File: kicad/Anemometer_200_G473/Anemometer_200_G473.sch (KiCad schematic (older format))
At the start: 147 parts, among them J1 Conn_01x01_Female, J11 USB_B_Micro, J13 Conn_01x01_Female, J15 Conn_01x01_Female, J16 Conn_01x01_Female, J17 Conn_01x01_Female, J18 Conn_01x01_Female, J19 Conn_01x01_Female, J2 Conn_01x01_Female, J20 Conn_01x01_Female, J21 Conn_01x01_Female, J22 Conn_01x01_Female, J23 Conn_01x01_Female, J24 Conn_01x01_Female, J3 Conn_01x08_Shielded, J4 Conn_01x01_Female, J5 Conn_01x01_Female, J6 Conn_01x01_Female, J7 Conn_01x01_Female, J8 Conn_01x04_Shielded, J9 Conn_01x01_Female, Q1 Q_NMOS_GSD, Q2 Q_NMOS_GSD, Q3 Q_NMOS_GSD, Q4 Q_NMOS_GSD, Q5 IRF7343PBF, Q6 IRF7343PBF, Q7 IRF7343PBF, Q8 IRF7343PBF, U1 W5500, U2 NCP1117-3.3, U3 TS5A23159DGS, U4 TS5A23159DGS, Y1 16, Y2 Crystal_GND24_Small

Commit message: изменено:      kicad/Anemometer_200_G473/Anemometer_200_G473-cache.lib 	изменено:      kicad/Anemometer_200_G473/Anemometer_200_G473.kicad_pcb 	изменено:      kicad/Anemometer_200_G473/Anemometer_200_G473.kicad_pcb-bak 	изменено:      kicad/Anemometer_200_G473/Anemometer_200_G473.sch 	изменено:      kicad/Anemometer_200_G473/Anemometer_200_G473.sch-bak
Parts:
- D10: symbol Anemometer_200_G473-rescue:AD5245-My_Library-My_Library -> Anemometer_200_G473-rescue:AD5245-My_Library-My_Library-Anemometer_200_G473-rescue
- D2: symbol Anemometer_200_G473-rescue:STM32G473CBTx-My_Library-Anemometer_200_G473-rescue -> Anemometer_200_G473-rescue:STM32G473CBTx-My_Library-Anemometer_200_G473-rescue-Anemometer_200_G473-rescue
- D5: symbol Anemometer_200_G473-rescue:CH340N-My_Library-Anemometer_200_G473-rescue -> Anemometer_200_G473-rescue:CH340N-My_Library-Anemometer_200_G473-rescue-Anemometer_200_G473-rescue
- D9: symbol Anemometer_200_G473-rescue:MAX4477-My_Library -> Anemometer_200_G473-rescue:MAX4477-My_Library-Anemometer_200_G473-rescue
- J3: symbol Anemometer_200_G473-rescue:Conn_01x08_Shielded-My_Library-Anemometer_200_G473-rescue -> Anemometer_200_G473-rescue:Conn_01x08_Shielded-My_Library-Anemometer_200_G473-rescue-Anemometer_200_G473-rescue
- J8: symbol Anemometer_200_G473-rescue:Conn_01x04_Shielded-My_Library-Anemometer_200_G473-rescue -> Anemometer_200_G473-rescue:Conn_01x04_Shielded-My_Library-Anemometer_200_G473-rescue-Anemometer_200_G473-rescue
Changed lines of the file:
@@
 $EndDescr
 $Comp
-L Anemometer_200_G473-rescue:STM32G473CBTx-My_Library-Anemometer_200_G473-rescue D2
+L Anemometer_200_G473-rescue:STM32G473CBTx-My_Library-Anemometer_200_G473-rescue-Anemometer_200_G473-rescue D2
 U 1 1 645A79A7
 P 8000 2250
@@
 NoConn ~ 8700 1950
 $Comp
-L Anemometer_200_G473-rescue:CH340N-My_Library-Anemometer_200_G473-rescue D5
+L Anemometer_200_G473-rescue:CH340N-My_Library-Anemometer_200_G473-rescue-Anemometer_200_G473-rescue D5
 U 1 1 6496EE1B
 P 9950 2850
@@
 $EndComp
 $Comp
-L Anemometer_200_G473-rescue:Conn_01x08_Shielded-My_Library-Anemometer_200_G473-rescue J3
+L Anemometer_200_G473-rescue:Conn_01x08_Shielded-My_Library-Anemometer_200_G473-rescue-Anemometer_200_G473-rescue J3
 U 1 1 65094C58
 P 5450 1800
@@
 $EndComp
 $Comp
-L Anemometer_200_G473-rescue:Conn_01x04_Shielded-My_Library-Anemometer_200_G473-rescue J8
+L Anemometer_200_G473-rescue:Conn_01x04_Shielded-My_Library-Anemometer_200_G473-rescue-Anemometer_200_G473-rescue J8
 U 1 1 648B00AE
 P 6200 900
@@
 $EndComp
 $Comp
-L Anemometer_200_G473-rescue:MAX4477-My_Library D9
+L Anemometer_200_G473-rescue:MAX4477-My_Library-Anemometer_200_G473-rescue D9
 U 1 1 64A019B6
 P 8050 5150
@@
 $EndComp
 $Comp
-L Anemometer_200_G473-rescue:MAX4477-My_Library D9
+L Anemometer_200_G473-rescue:MAX4477-My_Library-Anemometer_200_G473-rescue D9
 U 2 1 64A0390D
 P 10050 5800
@@
 $EndComp
 $Comp
-L Anemometer_200_G473-rescue:AD5245-My_Library-My_Library D10
+L Anemometer_200_G473-rescue:AD5245-My_Library-My_Library-Anemometer_200_G473-rescue D10
 U 1 1 64A1FA03
 P 8650 5550

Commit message: изменено:      kicad/Anemometer_200_G473/Anemometer_200_G473-cache.lib 	изменено:      kicad/Anemometer_200_G473/Anemometer_200_G473.sch 	изменено:      kicad/Anemometer_200_G473/Anemometer_200_G473.sch-bak 	изменено:      stm32cubeide/Anemometer_G474CBT6_MATLAB/.mxproject 	изменено:      stm32cubeide/Anemometer_G474CBT6_MATLAB/.settings/language.settings.xml 	изменено:      stm32cubeide/Anemometer_G474CBT6_MATLAB/Anemometer_G473CBT7_MATLAB.ioc 	изменено:      stm32cubeide/Anemometer_G474CBT6_MATLAB/Core/Inc/main.h 	изменено:      stm32cubeide/Anemometer_G474CBT6_MATLAB/Core/Inc/stm32g4xx_hal_conf.h 	изменено:      stm32cubeide/Anemometer_G474CBT6_MATLAB/Core/Src/main.c 	изменено:      stm32cubeide/Anemometer_G474CBT6_MATLAB/Debug/Anemometer_G473CBT7_MATLAB.elf 	изменено:      stm32cubeide/Anemometer_G474CBT6_MATLAB/Debug/Anemometer_G473CBT7_MATLAB.list 	изменено:      stm32cubeide/Anemometer_G474CBT6_MATLAB/Debug/Anemometer_G473CBT7_MATLAB.map 	изменено:      stm32cubeide/Anemometer_G474CBT6_MATLAB/Debug/Core/Src/main.cyclo 	изменено:      stm32cubeide/Anemometer_G474CBT6_MATLAB/Debug/Core/Src/main.d 	изменено:      stm32cubeide/Anemometer_G474CBT6_MATLAB/Debug/Core/Src/main.o 	изменено:      stm32cubeide/Anemometer_G474CBT6_MATLAB/Debug/Core/Src/main.su 	изменено:      stm32cubeide/Anemometer_G474CBT6_MATLAB/Debug/Core/Src/stm32g4xx_hal_msp.cyclo 	изменено:      stm32cubeide/Anemometer_G474CBT6_MATLAB/Debug/Core/Src/stm32g4xx_hal_msp.d 	изменено:      stm32cubeide/Anemometer_G474CBT6_MATLAB/Debug/Core/Src/stm32g4xx_hal_msp.o 	изменено:      stm32cubeide/Anemometer_G474CBT6_MATLAB/Debug/Core/Src/stm32g4xx_hal_msp.su 	изменено:      stm32cubeide/Anemometer_G474CBT6_MATLAB/Debug/Core/Src/stm32g4xx_it.cyclo 	изменено:      stm32cubeide/Anemometer_G474CBT6_MATLAB/Debug/Core/Src/stm32g4xx_it.d 	изменено:      stm32cubeide/Anemometer_G474CBT6_MATLAB/Debug/Core/Src/stm32g4xx_it.o 	изменено:      stm32cubeide/Anemometer_G474CBT6_MATLAB/Debug/Core/Src/stm32g4xx_it.su 	измен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
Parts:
- D10: symbol Anemometer_200_G473-rescue:AD5245-My_Library-My_Library-Anemometer_200_G473-rescue -> Anemometer_200_G473-rescue:AD5245-My_Library-My_Library-Anemometer_200_G473-rescue-Anemometer_200_G473-rescue
- D2: symbol Anemometer_200_G473-rescue:STM32G473CBTx-My_Library-Anemometer_200_G473-rescue-Anemometer_200_G473-rescue -> Anemometer_200_G473-rescue:STM32G473CBTx-My_Library-Anemometer_200_G473-rescue-Anemometer_200_G473-rescue-Anemometer_20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
- D5: symbol Anemometer_200_G473-rescue:CH340N-My_Library-Anemometer_200_G473-rescue-Anemometer_200_G473-rescue -> Anemometer_200_G473-rescue:CH340N-My_Library-Anemometer_200_G473-rescue-Anemometer_200_G473-rescue-Anemometer_200_G473-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
- D9: symbol Anemometer_200_G473-rescue:MAX4477-My_Library-Anemometer_200_G473-rescue -> Anemometer_200_G473-rescue:MAX4477-My_Library-Anemometer_200_G473-rescue-Anemometer_200_G473-rescue
- J3: symbol Anemometer_200_G473-rescue:Conn_01x08_Shielded-My_Library-Anemometer_200_G473-rescue-Anemometer_200_G473-rescue -> Anemometer_200_G473-rescue:Conn_01x08_Shielded-My_Library-Anemometer_200_G473-rescue-Anemometer_200_G473-rescue-Anemome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
- J8: symbol Anemometer_200_G473-rescue:Conn_01x04_Shielded-My_Library-Anemometer_200_G473-rescue-Anemometer_200_G473-rescue -> Anemometer_200_G473-rescue:Conn_01x04_Shielded-My_Library-Anemometer_200_G473-rescue-Anemometer_200_G473-rescue-Anemome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
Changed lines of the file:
@@
 $EndDescr
 $Comp
-L Anemometer_200_G473-rescue:STM32G473CBTx-My_Library-Anemometer_200_G473-rescue-Anemometer_200_G473-rescue D2
+L Anemometer_200_G473-rescue:STM32G473CBTx-My_Library-Anemometer_200_G473-rescue-Anemometer_200_G473-rescue-Anemometer_200_G473-rescue D2
 U 1 1 645A79A7
 P 8000 2250
@@
 NoConn ~ 8700 1950
 $Comp
-L Anemometer_200_G473-rescue:CH340N-My_Library-Anemometer_200_G473-rescue-Anemometer_200_G473-rescue D5
+L Anemometer_200_G473-rescue:CH340N-My_Library-Anemometer_200_G473-rescue-Anemometer_200_G473-rescue-Anemometer_200_G473-rescue D5
 U 1 1 6496EE1B
 P 9950 2850
@@
 $EndComp
 $Comp
-L Anemometer_200_G473-rescue:Conn_01x08_Shielded-My_Library-Anemometer_200_G473-rescue-Anemometer_200_G473-rescue J3
+L Anemometer_200_G473-rescue:Conn_01x08_Shielded-My_Library-Anemometer_200_G473-rescue-Anemometer_200_G473-rescue-Anemometer_200_G473-rescue J3
 U 1 1 65094C58
 P 5450 1800
@@
 $EndComp
 $Comp
-L Anemometer_200_G473-rescue:Conn_01x04_Shielded-My_Library-Anemometer_200_G473-rescue-Anemometer_200_G473-rescue J8
+L Anemometer_200_G473-rescue:Conn_01x04_Shielded-My_Library-Anemometer_200_G473-rescue-Anemometer_200_G473-rescue-Anemometer_200_G473-rescue J8
 U 1 1 648B00AE
 P 6200 900
@@
 $EndComp
 $Comp
-L Anemometer_200_G473-rescue:MAX4477-My_Library-Anemometer_200_G473-rescue D9
+L Anemometer_200_G473-rescue:MAX4477-My_Library-Anemometer_200_G473-rescue-Anemometer_200_G473-rescue D9
 U 1 1 64A019B6
 P 8050 5150
@@
 $EndComp
 $Comp
-L Anemometer_200_G473-rescue:MAX4477-My_Library-Anemometer_200_G473-rescue D9
+L Anemometer_200_G473-rescue:MAX4477-My_Library-Anemometer_200_G473-rescue-Anemometer_200_G473-rescue D9
 U 2 1 64A0390D
 P 10050 5800
@@
 $EndComp
 $Comp
-L Anemometer_200_G473-rescue:AD5245-My_Library-My_Library-Anemometer_200_G473-rescue D10
+L Anemometer_200_G473-rescue:AD5245-My_Library-My_Library-Anemometer_200_G473-rescue-Anemometer_200_G473-rescue D10
 U 1 1 64A1FA03
 P 8650 5550

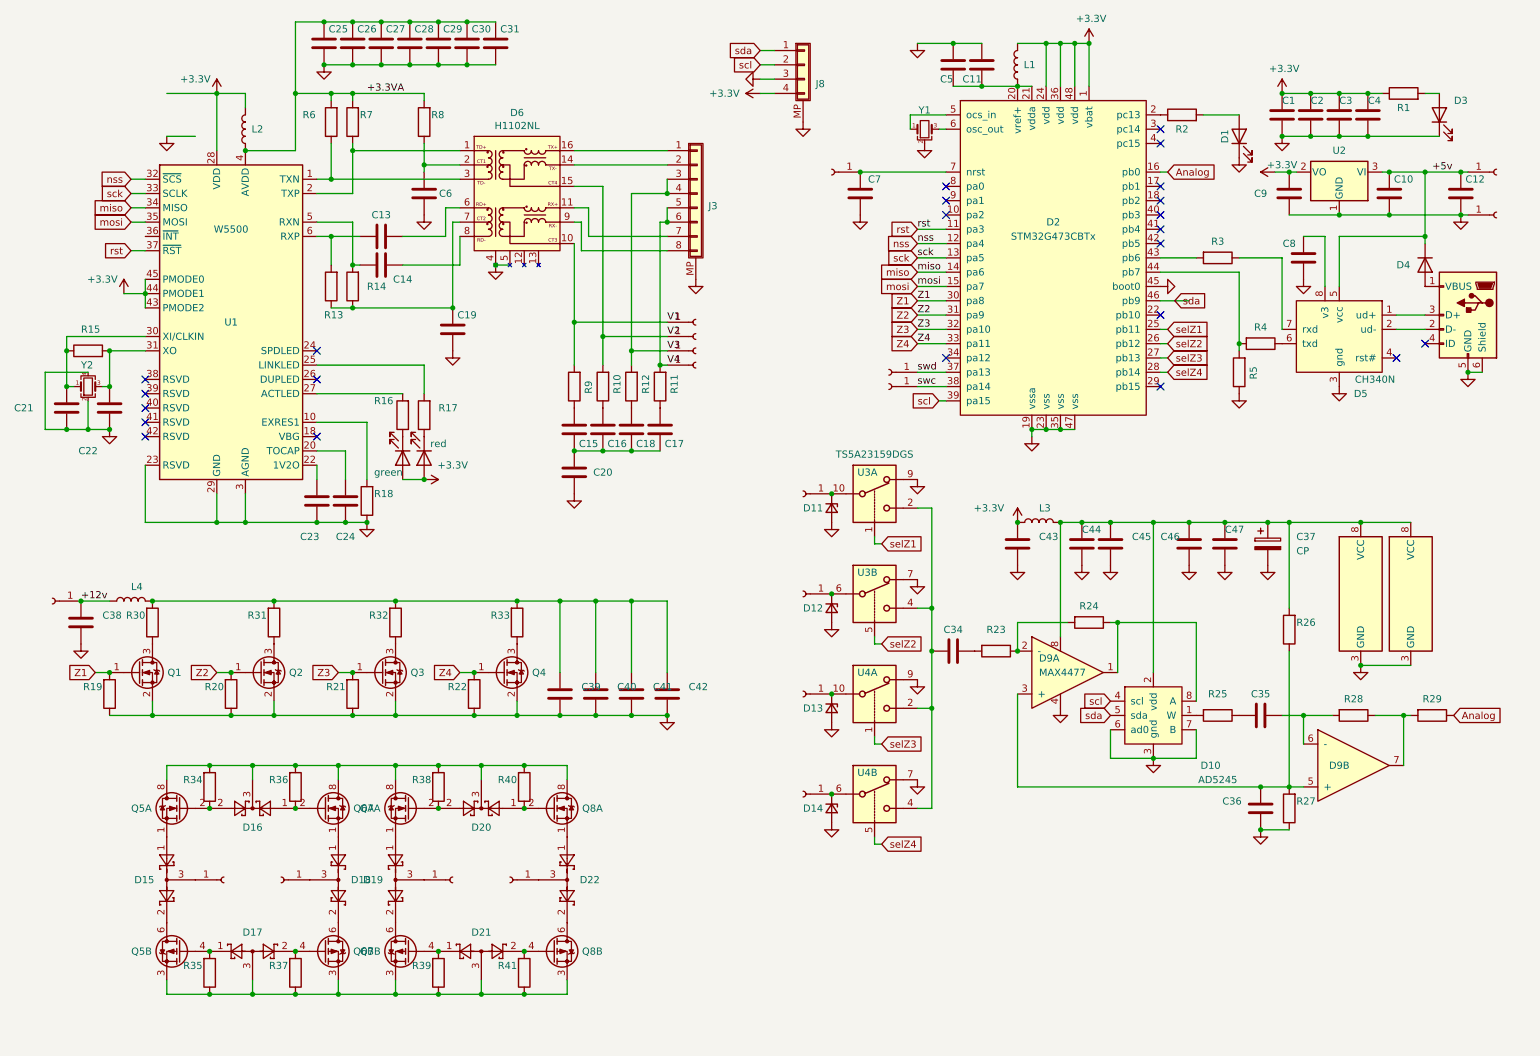
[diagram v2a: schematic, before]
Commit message: изменено:      kicad/Anemometer_200_G473/Anemometer_200_G473-cache.lib 	изменено:      kicad/Anemometer_200_G473/Anemometer_200_G473.sch 	изменено:      kicad/Anemometer_200_G473/Anemometer_200_G473.sch-bak 	изменено:      stm32cubeide/Anemometer_G474CBT6_MATLAB/Anemometer_G473CBT7_MATLAB.ioc 	изменено:      stm32cubeide/Anemometer_G474CBT6_MATLAB/Core/Inc/main.h 	изменено:      stm32cubeide/Anemometer_G474CBT6_MATLAB/Core/Src/main.c 	изменено:      stm32cubeide/Anemometer_G474CBT6_MATLAB/Core/Src/stm32g4xx_hal_msp.c 	изменено:      stm32cubeide/Anemometer_G474CBT6_MATLAB/Debug/Anemometer_G473CBT7_MATLAB.elf 	изменено:      stm32cubeide/Anemometer_G474CBT6_MATLAB/Debug/Anemometer_G473CBT7_MATLAB.list 	изменено:      stm32cubeide/Anemometer_G474CBT6_MATLAB/Debug/Anemometer_G473CBT7_MATLAB.map 	изменено:      stm32cubeide/Anemometer_G474CBT6_MATLAB/Debug/Core/Src/main.o 	изменено:      stm32cubeide/Anemometer_G474CBT6_MATLAB/Debug/Core/Src/stm32g4xx_hal_msp.o 	изменено:      stm32cubeide/Anemometer_G474CBT6_MATLAB/Debug/Core/Src/stm32g4xx_it.o 	изменено:      stm32cubeide/Anemometer_G474CBT6_MATLAB/Release/Anemometer_G473CBT7_MATLAB.elf 	изменено:      stm32cubeide/Anemometer_G474CBT6_MATLAB/Release/Anemometer_G473CBT7_MATLAB.list 	изменено:      stm32cubeide/Anemometer_G474CBT6_MATLAB/Release/Anemometer_G473CBT7_MATLAB.map 	изменено:      stm32cubeide/Anemometer_G474CBT6_MATLAB/Release/Core/Src/main.o 	изменено:      stm32cubeide/Anemometer_G474CBT6_MATLAB/Release/Core/Src/stm32g4xx_hal_msp.o
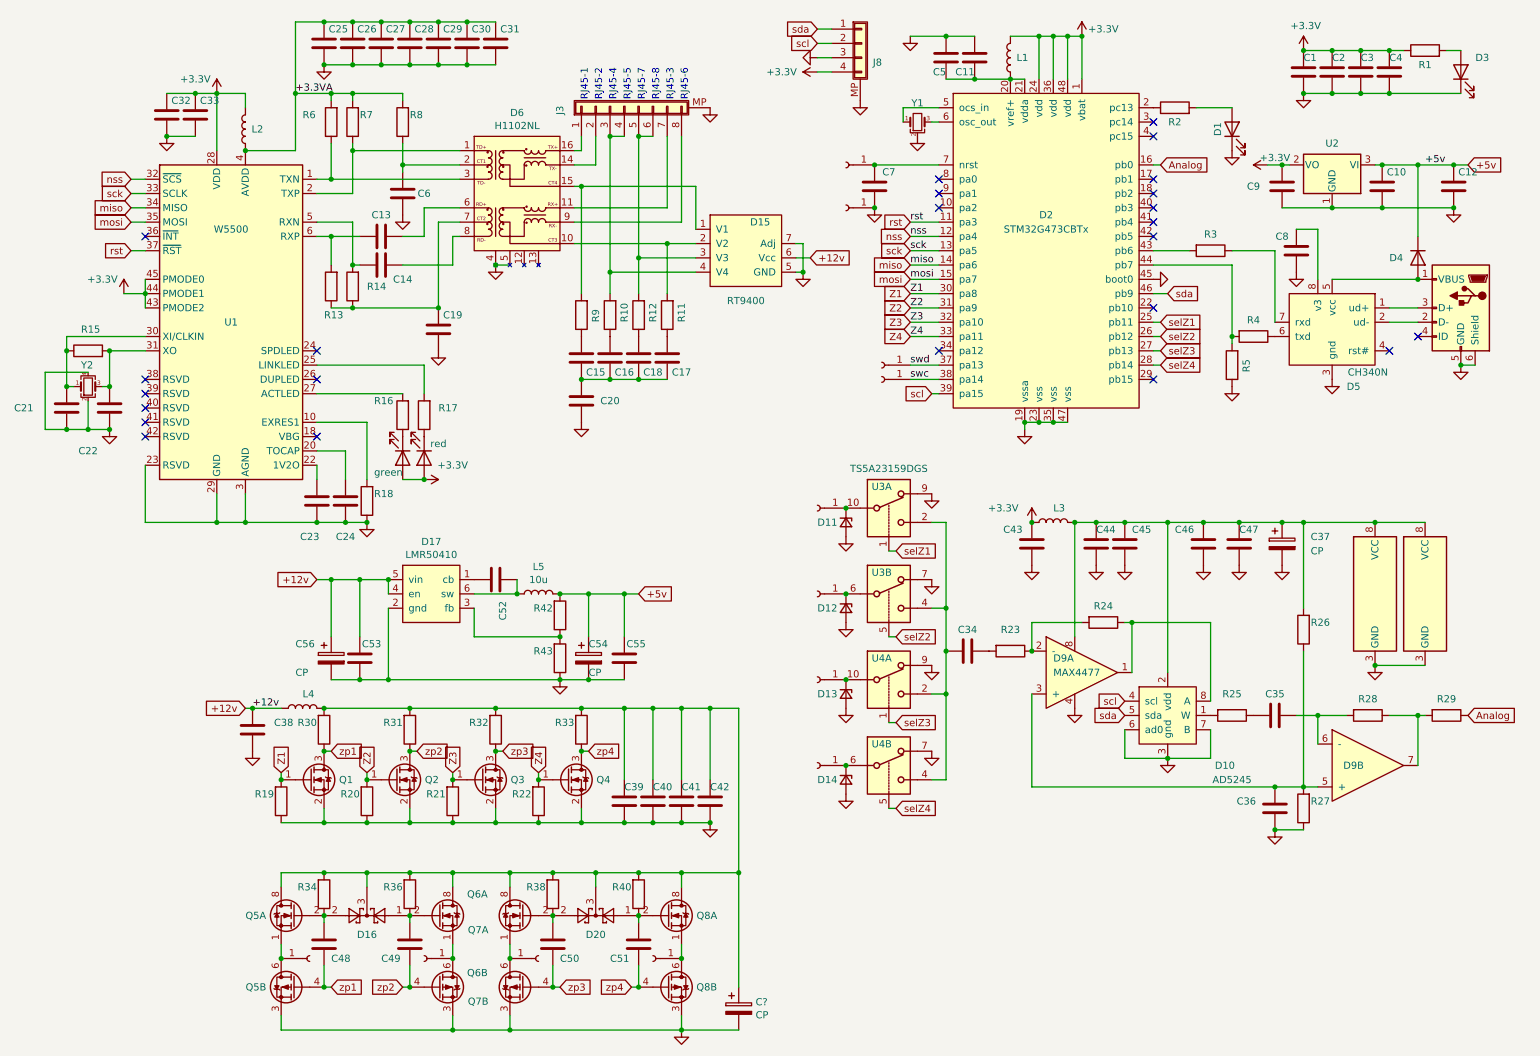
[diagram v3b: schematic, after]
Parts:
- removed D15, D18, D19, D22: BAT54S, Package_TO_SOT_SMD:SOT-23, symbol Diode:BAT54S
- removed D17, D21: BAT54A, Package_TO_SOT_SMD:SOT-23, symbol Diode:BAT54A
- removed J18, J19, J4, J5, J6, J7, J9: Conn_01x01_Female, My-library:mini_conn, symbol Connector:Conn_01x01_Female
- removed R35, R37, R39, R41: 12.4k, Resistor_SMD:R_0402_1005Metric, symbol Device:R
- added C32, C33: 22n, Capacitor_SMD:C_0402_1005Metric, symbol Device:C
- added C48, C49, C50, C51, C52: 85n, Capacitor_SMD:C_0603_1608Metric, symbol Device:C
- added C53, C55: C, Capacitor_SMD:C_0805_2012Metric, symbol Device:C
- added C54, C56, C?: CP, Capacitor_Tantalum_SMD:CP_EIA-7343-40_Kemet-Y_Pad2.25x2.55mm_HandSolder, symbol Device:CP
- added D15: RT9400, My-library:TR9400, symbol My_Library:RT9400
- added D17: LMR50410, Package_TO_SOT_SMD:SOT-23-6, symbol My_Library:LMR50410
- added J?: Conn_01x01_Female, My-library:mini_conn, symbol Connector:Conn_01x01_Female
- added L5: 10u, Inductor_SMD:L_Bourns_SRP7028A_7.3x6.6mm, symbol Device:L
- added R42, R43: 12.4k, Resistor_SMD:R_0402_1005Metric, symbol Device:R
- C37: footprint (none) -> Capacitor_Tantalum_SMD:CP_EIA-7343-40_Kemet-Y_Pad2.25x2.55mm_HandSolder
- C39, C40, C41, C42: footprint Capacitor_SMD:C_0603_1608Metric -> Capacitor_SMD:C_0805_2012Metric
- L2, L4: value L -> 10u
- L3: value L -> 47u
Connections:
- net +12v: now also C53.2, C56.1, D15.6 (Vcc), D17.4 (en), D17.5 (vin)
- net +3V3: now also C32.1, C33.1
- net +5v: now also C54.1, C55.2, L5.2, R42.2; no longer D5.5 (vcc)
- net GND: now also Q5.3 (1), Q6.3 (1), Q7.3 (1), Q8.3 (1), C32.2, C33.2, C53.1, C54.2, C55.1, C56.2, C?.2, D15.5 (GND), D15.7 (Adj), D17.2 (gnd), J?.1 (Pin_1), R43.1
- net at D4.2 (A), J11.1 (VBUS): now also D5.5 (vcc)
- net zp1: now reaches Q5.4 (G)
- net zp1: now also Q1.3 (D), R30.1, C48.2
- net at Q5.5 (D), Q5.6 (D): now also J2.1 (Pin_1), Q5.1 (S)
- net at D16.2, Q5.2 (G), R34.1: now also C48.1
- net at D16.3, D20.3, Q5.7 (D)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: now also C39.1, C40.1, C41.1, C42.1, L4.2, R30.2, R31.2, R32.2, R33.2, C?.1
- net at Q6.1 (S): now also J15.1 (Pin_1), Q6.5 (D), Q6.6 (D)
- net at D16.1, Q6.2 (G), R36.1: now also C49.1
- net zp2: now reaches Q6.4 (G)
- net zp2: now also Q2.3 (D), R31.1, C49.2
- net at Q7.1 (S): now also J13.1 (Pin_1), Q7.5 (D), Q7.6 (D)
- net at D20.2, Q7.2 (G), R38.1: now also C50.1
- net zp3: now reaches Q7.4 (G)
- net zp3: now also Q3.3 (D), R32.1, C50.2
- net at Q8.1 (S): now also J16.1 (Pin_1), Q8.5 (D), Q8.6 (D)
- net at D20.1, Q8.2 (G), R40.1: now also C51.1
- net zp4: now reaches Q8.4 (G)
- net zp4: now also Q4.3 (D), R33.1, C51.2
- net V1: no longer names the net of D6.10
- net V1: now also R11.2, D15.2 (V2); no longer R9.2
- net V2: no longer names the net of D6.15
- net V2: now also R9.2, D15.1 (V1); no longer R10.2
- net V3: no longer names the net of J3.3 (Pin_3), J3.4 (Pin_4)
- net V3: now also R10.2, D15.4 (V4); no longer R12.2
- net V4: no longer names the net of J3.5 (Pin_5), J3.6 (Pin_6)
- net V4: now also R12.2, D15.3 (V3); no longer R11.2
- new net: C52.2, D17.1 (cb)
- new net: D17.3 (fb), R42.1, R43.2
- new net: C52.1, D17.6 (sw), L5.1
- no-connect marks 23 -> 24
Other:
- note added: "RJ45-1"
- note added: "RJ45-2"
- note added: "RJ45-3"
- note added: "RJ45-4"
- note added: "RJ45-5"
- note added: "RJ45-6"
- note added: "RJ45-7"
- note added: "RJ45-8"
- moved on the sheet: C1, C10, C11, C12, C15, C16, C17, C18, C19, C2, C20, C3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
